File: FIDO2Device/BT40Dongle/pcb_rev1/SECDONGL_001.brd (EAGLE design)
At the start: 20 x 30 mm, 38 parts, among them CN1 CX60-24S-UNIT, CN2 IF_5PIN_H, CN3 IF_2PIN_SOL, SW1 SKRPACE010, SW2 SKRPACE010, SW3 SKTADAE010, U1 BT40, U2 ADP122ACPZ-3.3-R7, U3 RV-3028-C7

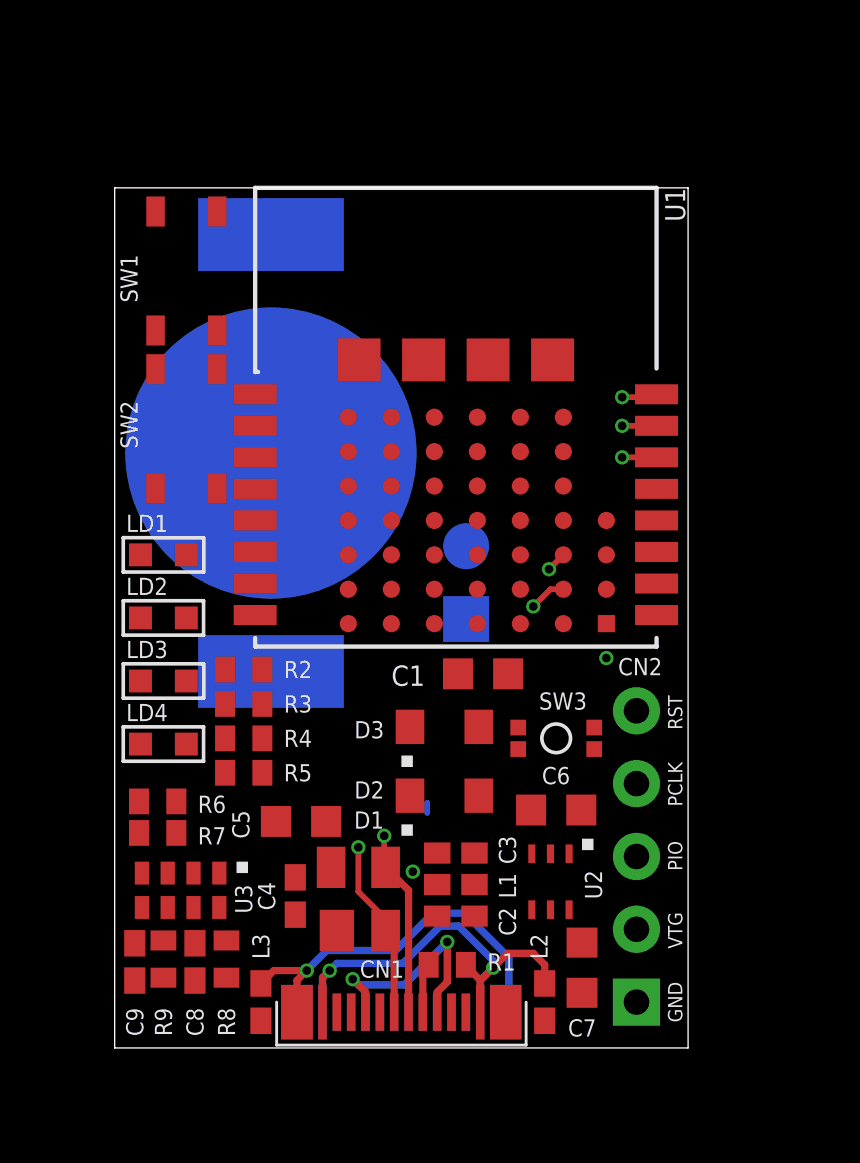
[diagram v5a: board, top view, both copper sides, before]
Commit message: 配線レイアウトを作成
・レイヤー設定を変更（１〜２面間でブラインドviaが使用できるよう修正）
・一部の貫通viaを、ブラインドviaに変更
・電池ケースの位置を調整
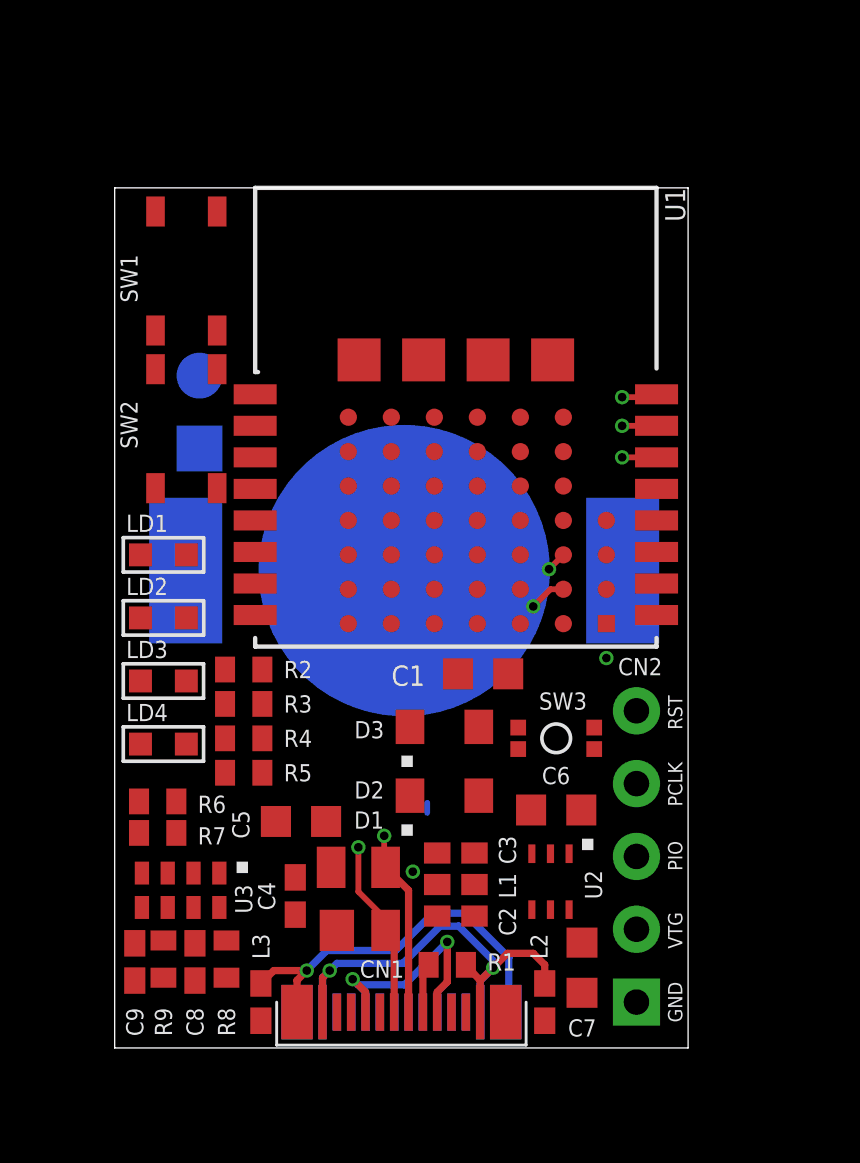
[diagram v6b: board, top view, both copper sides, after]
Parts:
- moved CN3 11.0 mm to (2.96, 20.9)
- moved BAT1 6.20 mm to (10.1, 16.6), turned to 180 degrees
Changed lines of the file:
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@@
 <layers>
 <layer number="1" name="Top" color="4" fill="1" visible="yes" active="yes"/>
-<layer number="2" name="Route2" color="1" fill="3" visible="yes" active="yes"/>
+<layer number="2" name="Route2" color="10" fill="3" visible="yes" active="yes"/>
 <layer number="3" name="Route3" color="4" fill="3" visible="no" active="no"/>
 <layer number="14" name="Route14" color="1" fill="6" visible="no" active="no"/>
@@
 design rules under a new name.
 </description>
-<param name="layerSetup" value="(1*2*15*16)"/>
-<param name="mtCopper" value="0.035mm 0.0175mm 0.035mm 0.035mm 0.035mm 0.035mm 0.035mm 0.035mm 0.035mm 0.035mm 0.035mm 0.035mm 0.035mm 0.035mm 0.0175mm 0.035mm"/>
-<param name="mtIsolate" value="0.2mm 0.3mm 0.2mm 0.15mm 0.2mm 0.15mm 0.2mm 0.15mm 0.2mm 0.15mm 0.2mm 0.15mm 0.2mm 0.15mm 0.2mm"/>
+<param name="layerSetup" value="[2:(1*2+15*16)]"/>
+<param name="mtCopper" value="0.035mm 0.035mm 0.035mm 0.035mm 0.035mm 0.035mm 0.035mm 0.035mm 0.035mm 0.035mm 0.035mm 0.035mm 0.035mm 0.035mm 0.035mm 0.035mm"/>
+<param name="mtIsolate" value="0.15mm 0.15mm 0.2mm 0.15mm 0.2mm 0.15mm 0.2mm 0.15mm 0.2mm 0.15mm 0.2mm 0.15mm 0.2mm 0.15mm 0.15mm"/>
 <param name="mdWireWire" value="6mil"/>
 <param name="mdWirePad" value="6mil"/>
@@
 </autorouter>
 <elements>
-<element name="BAT1" library="Connectors" package="BAT-HLD-012-SMT" value="BAT-HLD-012-SMT" x="5.45" y="20.75" smashed="yes" rot="MR90">
-<attribute name="NAME" x="8.65" y="27.2" size="0.7" layer="26" rot="MR90"/>
-<attribute name="VALUE" x="6.24" y="30.58" size="0.7" layer="28" rot="MR90"/>
+<element name="BAT1" library="Connectors" package="BAT-HLD-012-SMT" value="BAT-HLD-012-SMT" x="10.1" y="16.65" smashed="yes" rot="MR180">
+<attribute name="NAME" x="3" y="13.1" size="0.7" layer="26" rot="MR180"/>
+<attribute name="VALUE" x="19.93" y="15.86" size="0.7" layer="28" rot="MR180"/>
 </element>
 <element name="C1" library="Parts" package="C0603K" value="4.7uF" x="12.85" y="13.05" smashed="yes">
@@
 <attribute name="VALUE" x="3.95" y="7.6" size="0.7112" layer="27" rot="R180"/>
 </element>
-<element name="CN3" library="Connectors" package="SOLPAD_2PIN" value="IF_2PIN_SOL" x="12.26" y="14.96" smashed="yes" rot="MR90">
-<attribute name="NAME" x="10.83" y="17.19" size="0.889" layer="26" ratio="11" rot="MR270"/>
-<attribute name="VALUE" x="10.99" y="13.69" size="0.889" layer="28" ratio="11" rot="MR90" align="top-left"/>
+<element name="CN3" library="Connectors" package="SOLPAD_2PIN" value="IF_2PIN_SOL" x="2.96" y="20.91" smashed="yes" rot="MR90">
+<attribute name="NAME" x="1.53" y="23.14" size="0.889" layer="26" ratio="11" rot="MR270"/>
+<attribute name="VALUE" x="1.69" y="19.64" size="0.889" layer="28" ratio="11" rot="MR90" align="top-left"/>
 </element>
 </elements>
@@
 <wire x1="10.775" y1="24" x2="11.15" y2="22" width="0" layer="19" extent="1-1"/>
 <wire x1="8.525" y1="24" x2="10.775" y2="24" width="0" layer="19" extent="1-1"/>
-<wire x1="5.45" y1="20.75" x2="9.65" y2="22" width="0" layer="19" extent="1-16"/>
-<wire x1="1.425" y1="19.525" x2="5.45" y2="20.75" width="0" layer="19" extent="1-16"/>
-<wire x1="1.425" y1="23.675" x2="1.425" y2="19.525" width="0" layer="19" extent="1-1"/>
-<wire x1="1.425" y1="25.025" x2="1.425" y2="23.675" width="0" layer="19" extent="1-1"/>
-<wire x1="1.425" y1="29.175" x2="1.425" y2="25.025" width="0" layer="19" extent="1-1"/>
-<wire x1="12.26" y1="14.96" x2="12.65" y2="22" width="0" layer="19" extent="1-16"/>
-<wire x1="13.725" y1="13.05" x2="12.26" y2="14.96" width="0" layer="19" extent="1-16"/>
+<wire x1="10.1" y1="16.65" x2="9.65" y2="22" width="0" layer="19" extent="1-16"/>
+<wire x1="13.725" y1="13.05" x2="10.1" y2="16.65" width="0" layer="19" extent="1-16"/>
 <wire x1="14.075" y1="11.175" x2="13.725" y2="13.05" width="0" layer="19" extent="1-1"/>
 <wire x1="14.075" y1="10.425" x2="14.075" y2="11.175" width="0" layer="19" extent="1-1"/>
@@
 <wire x1="5.625" y1="7.9" x2="6.3" y2="4.65" width="0" layer="19" extent="1-1"/>
 <wire x1="18.9" y1="16.2" x2="13.725" y2="13.05" width="0" layer="19" extent="1-1"/>
+<wire x1="2.96" y1="20.91" x2="8.525" y2="24" width="0" layer="19" extent="1-16"/>
+<wire x1="1.425" y1="19.525" x2="2.96" y2="20.91" width="0" layer="19" extent="1-16"/>
+<wire x1="1.425" y1="23.675" x2="2.96" y2="20.91" width="0" layer="19" extent="1-16"/>
+<wire x1="1.425" y1="25.025" x2="1.425" y2="23.675" width="0" layer="19" extent="1-1"/>
+<wire x1="1.425" y1="29.175" x2="1.425" y2="25.025" width="0" layer="19" extent="1-1"/>
 </signal>
 <signal name="VBUS_NRF">
@@
 <contactref element="U1" pad="14"/>
 <contactref element="CN2" pad="5"/>
-<via x="17.7" y="20.6" extent="1-16" drill="0.3"/>
+<via x="17.7" y="20.6" extent="1-2" drill="0.3"/>
 <wire x1="17.7" y1="20.6" x2="16.5" y2="19.4" width="0.2032" layer="2"/>
 <wire x1="16.5" y1="19.4" x2="16.5" y2="13.46" width="0.2032" layer="2"/>
@@
 <contactref element="U1" pad="16"/>
 <contactref element="CN2" pad="3"/>
-<via x="17.7" y="22.7" extent="1-16" drill="0.3"/>
+<via x="17.7" y="22.7" extent="1-2" drill="0.3"/>
 <wire x1="17.7" y1="22.7" x2="15.7" y2="20.7" width="0.2032" layer="2"/>
 <wire x1="15.7" y1="20.7" x2="15.7" y2="9.18" width="0.2032" layer="2"/>
@@
 <contactref element="U1" pad="15"/>
 <contactref element="CN2" pad="4"/>
-<via x="17.7" y="21.7" extent="1-16" drill="0.3"/>
+<via x="17.7" y="21.7" extent="1-2" drill="0.3"/>
 <wire x1="17.7" y1="21.7" x2="16.1" y2="20.1" width="0.2032" layer="2"/>
 <wire x1="16.1" y1="20.1" x2="16.1" y2="11.32" width="0.2032" layer="2"/>
@@
 <wire x1="9.75" y1="1.25" x2="9.75" y2="3.8" width="0.254" layer="1"/>
 <wire x1="9.75" y1="3.8" x2="9.45" y2="4.1" width="0.254" layer="1"/>
-<via x="14.6" y="15.4" extent="1-16" drill="0.3"/>
+<via x="14.6" y="15.4" extent="1-2" drill="0.3"/>
 <wire x1="14.6" y1="15.4" x2="15.2" y2="16" width="0.2032" layer="1"/>
 <wire x1="15.2" y1="16" x2="15.65" y2="16" width="0.2032" layer="1"/>
 <wire x1="14.6" y1="15.4" x2="14.6" y2="13.7" width="0.2032" layer="2"/>
 <wire x1="14.6" y1="13.7" x2="8.5" y2="7.6" width="0.2032" layer="2"/>
-<via x="8.5" y="7" extent="1-16" drill="0.3"/>
+<via x="8.5" y="7" extent="1-2" drill="0.3"/>
 <wire x1="8.5" y1="7" x2="8.5" y2="7.6" width="0.2032" layer="2"/>
 <wire x1="8.5" y1="7" x2="8.5" y2="5.45" width="0.2032" layer="1"/>
@@
 <wire x1="9.45" y1="6.3" x2="9.5" y2="6.35" width="0.2032" layer="1"/>
 <wire x1="9.5" y1="6.35" x2="9.4" y2="6.45" width="0.254" layer="1"/>
-<via x="15.15" y="16.7" extent="1-16" drill="0.3"/>
+<via x="15.15" y="16.7" extent="1-2" drill="0.3"/>
 <wire x1="15.15" y1="16.7" x2="15.15" y2="13.5" width="0.2032" layer="2"/>
 <wire x1="15.65" y1="17.2" x2="15.15" y2="16.7" width="0.2032" layer="1"/>
 <wire x1="15.15" y1="13.5" x2="9.4" y2="7.75" width="0.2032" layer="2"/>
-<via x="9.4" y="7.4" extent="1-16" drill="0.3"/>
+<via x="9.4" y="7.4" extent="1-2" drill="0.3"/>
 <wire x1="9.4" y1="7.4" x2="9.4" y2="7.75" width="0.2032" layer="2"/>
 <wire x1="9.4" y1="7.4" x2="9.4" y2="6.35" width="0.2032" layer="1"/>
@@
 <contactref element="U1" pad="C5"/>
 <contactref element="CN3" pad="2"/>
-<wire x1="12.26" y1="17.5" x2="12.65" y2="16" width="0" layer="19" extent="1-16"/>
+<wire x1="2.96" y1="23.45" x2="12.65" y2="16" width="0" layer="19" extent="1-16"/>
 </signal>
 <signal name="SCL">
@@
 <contactref element="D3" pad="A"/>
 <contactref element="R9" pad="2"/>
-<wire x1="12.7" y1="11.2" x2="5.45" y2="28.37" width="0" layer="19" extent="1-16"/>
+<wire x1="12.7" y1="11.2" x2="17.72" y2="16.65" width="0" layer="19" extent="1-16"/>
 <wire x1="1.7" y1="2.45" x2="12.7" y2="11.2" width="0" layer="19" extent="1-1"/>
 </signal>

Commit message: 配線レイアウトを作成
・べたGNDパターンを４面全てに追加
・電源の配線を第３面に追加
・その他、信号配線を第２面に追加
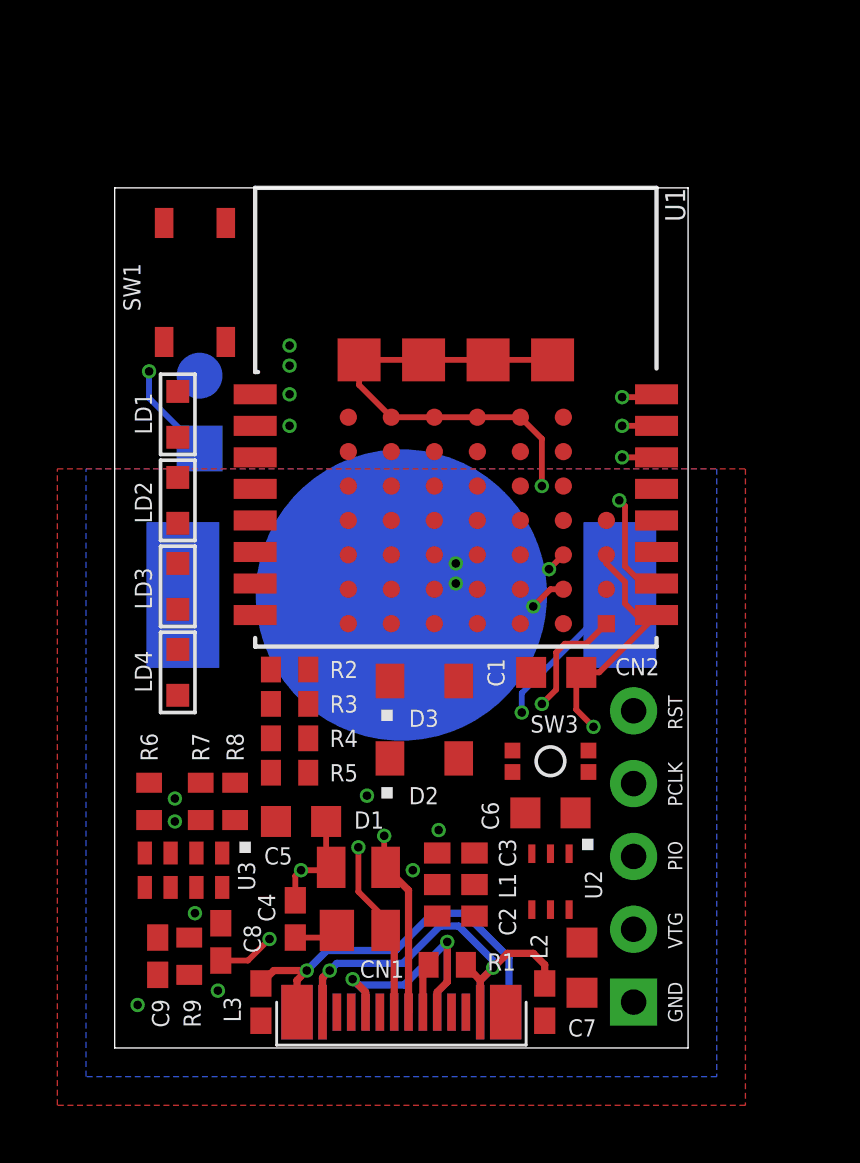
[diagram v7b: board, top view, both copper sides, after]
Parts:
- removed SW2: SKRPACE010, Parts:SKRPACE010
- moved R8 5.51 mm to (4.20, 8.60), turned to 270 degrees
- moved LD1 4.93 mm to (2.20, 22.1), turned to 90 degrees
- moved LD2 4.13 mm to (2.20, 19.1), turned to 90 degrees
- moved LD3 3.34 mm to (2.20, 16.1), turned to 90 degrees
- moved C1 2.55 mm to (15.4, 13.1), turned to 180 degrees
- moved LD4 2.55 mm to (2.20, 13.1), turned to 90 degrees
- moved R7 1.86 mm to (3.00, 8.60), turned to 90 degrees
- moved D3 1.75 mm to (10.8, 12.8)
- moved R2 1.60 mm to (6.10, 13.2)
- moved R3 1.60 mm to (6.10, 12.0)
- moved R4 1.60 mm to (6.10, 10.8)
- moved R5 1.60 mm to (6.10, 9.60)
- moved D2 1.48 mm to (10.8, 10.1)
- moved C8 1.14 mm to (3.70, 3.70)
- moved R9 0.91 mm to (2.60, 3.20)
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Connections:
- removed net SW2: SW2.1, SW2.2, U1.C3
- net 0V: no longer SW2.3, SW2.4
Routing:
- net 0V: track 0.00 -> 27.1 mm, vias 0 -> 5
- net VDD_NRF: track 0.00 -> 24.2 mm, vias 0 -> 3
- net VDD_BAT: track 0.00 -> 20.6 mm, vias 0 -> 2
- net VBUS_NRF: track 0.35 -> 10.5 mm, vias 1 -> 2
- net VBUS: track 11.9 -> 19.7 mm, vias 3 -> 4
- net SWCLK: track 15.2 -> 15.8 mm
- added copper zone on layer 1, net 0V
- added copper zone on layer 15, net 0V
- added copper zone on layer 16, net 0V
- added copper zone on layer 2, net 0V

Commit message: 配線レイアウトを作成
・電源系の配線を修正
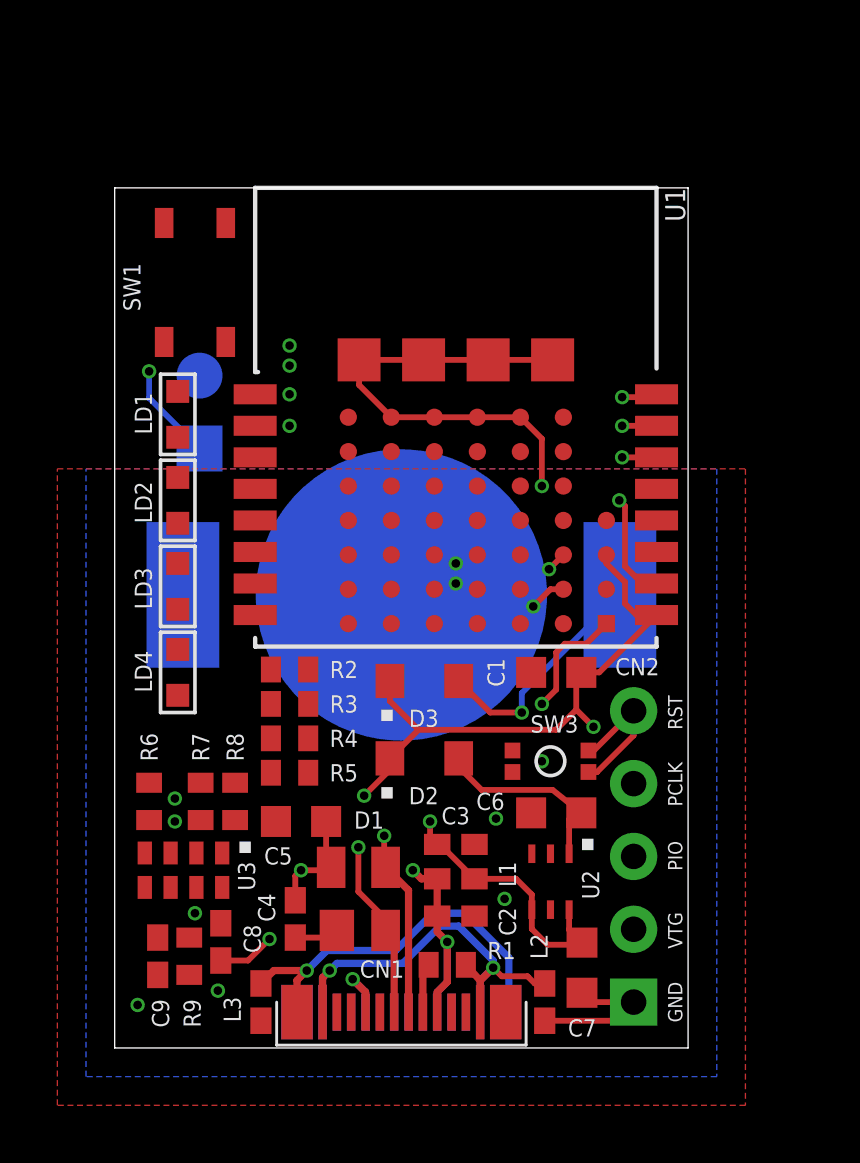
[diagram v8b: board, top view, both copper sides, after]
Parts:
- moved C3 0.30 mm to (11.9, 7.10)
- moved C6 0.20 mm to (15.4, 8.20)
- moved L1 0.20 mm to (11.9, 5.90)
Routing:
- net VDD_NRF: track 24.2 -> 35.1 mm
- net VBUS_NRF: track 10.5 -> 20.1 mm
- net N$3: track 0.00 -> 6.87 mm
- net 0V: track 27.1 -> 32.4 mm, vias 5 -> 8
- net RESET: track 11.2 -> 16.3 mm
- net VDD_BAT: track 20.6 -> 24.4 mm
- net VBUS: track 19.7 -> 23.0 mm
- net USB_GND: track 17.2 -> 16.4 mm
